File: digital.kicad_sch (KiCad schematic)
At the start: 29 parts, among them J1 Program Connector, J2 UART, J3 LCD ILI9488, SW1 Voltage, SW2 Current, U6 REF3030, U7 STM32G431CBTx

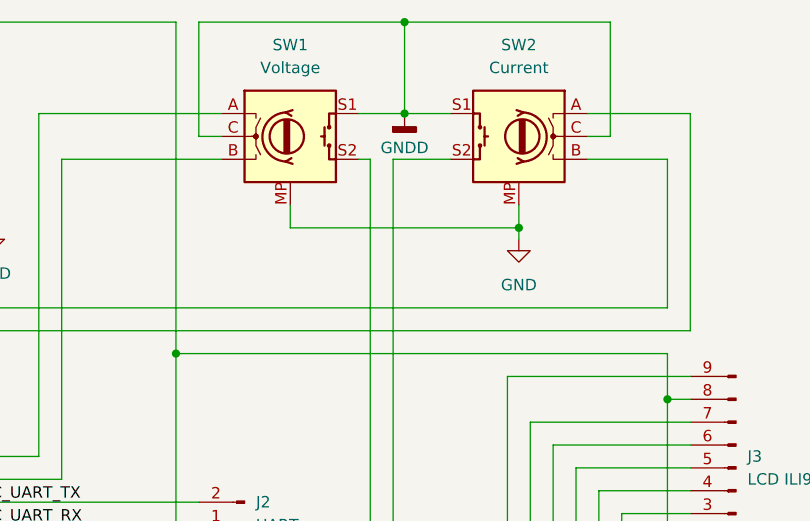
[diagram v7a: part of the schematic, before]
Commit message: Wstępne dodanie elementów na pcb oraz zmiana numeracji pinów do połączenia enkoderów. Zmiana symboli enkoderów na wersję bez masy i usunięcie zbędnego połączenia masy
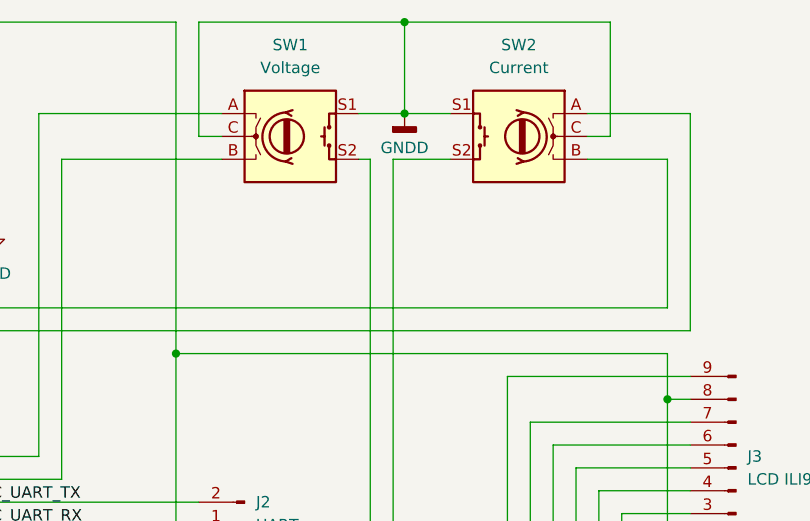
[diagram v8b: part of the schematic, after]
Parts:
- SW1, SW2: footprint (none) -> Connector_PinHeader_2.54mm:PinHeader_1x05_P2.54mm_Vertical; symbol Device:RotaryEncoder_Switch_MP -> Device:RotaryEncoder_Switch
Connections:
- net GND: no longer SW1.MP, SW2.MP
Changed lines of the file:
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@@
 		(color 0 0 0 0)
 	)
-	(junction
-		(at 222.25 41.91)
-		(diameter 0)
-		(color 0 0 0 0)
-	)
 	(no_connect
 		(at 125.73 85.09)
@@
 	(wire
 		(pts
-			(xy 222.25 41.91) (xy 222.25 39.37)
-		)
-		(stroke
-			(width 0)
-			(type default)
-		)
-	)
-	(wire
-		(pts
 			(xy 163.83 40.64) (xy 160.02 40.64)
 		)
@@
 	(wire
 		(pts
-			(xy 196.85 39.37) (xy 196.85 41.91)
-		)
-		(stroke
-			(width 0)
-			(type default)
-		)
-	)
-	(wire
-		(pts
 			(xy 186.69 19.05) (xy 209.55 19.05)
 		)
@@
 	(wire
 		(pts
-			(xy 196.85 41.91) (xy 222.25 41.91)
-		)
-		(stroke
-			(width 0)
-			(type default)
-		)
-	)
-	(wire
-		(pts
 			(xy 241.3 78.74) (xy 238.76 78.74)
 		)
@@
 	(wire
 		(pts
-			(xy 222.25 41.91) (xy 222.25 43.18)
-		)
-		(stroke
-			(width 0)
-			(type default)
-		)
-	)
-	(wire
-		(pts
 			(xy 246.38 105.41) (xy 246.38 110.49)
 		)
@@
 	)
 	(symbol
-		(lib_id "power:GND")
-		(at 222.25 43.18 0)
-		(unit 1)
-		(body_style 1)
-		(exclude_from_sim no)
-		(in_bom yes)
-		(on_board yes)
-		(in_pos_files yes)
-		(dnp no)
-		(fields_autoplaced yes)
-		(property "Reference" "#PWR027"
-			(at 222.25 49.53 0)
-			(hide yes)
-			(show_name no)
-			(do_not_autoplace no)
-			(effects
-				(font
-					(size 1.27 1.27)
-				)
-			)
-		)
-		(property "Value" "GND"
-			(at 222.25 48.26 0)
-			(show_name no)
-			(do_not_autoplace no)
-			(effects
-				(font
-					(size 1.27 1.27)
-				)
-			)
-		)
-		(property "Footprint" ""
-			(at 222.25 43.18 0)
-			(hide yes)
-			(show_name no)
-			(do_not_autoplace no)
-			(effects
-				(font
-					(size 1.27 1.27)
-				)
-			)
-		)
-		(property "Datasheet" ""
-			(at 222.25 43.18 0)
-			(hide yes)
-			(show_name no)
-			(do_not_autoplace no)
-			(effects
-				(font
-					(size 1.27 1.27)
-				)
-			)
-		)
-		(property "Description" "Power symbol creates a global label with name \"GND\" , ground"
-			(at 222.25 43.18 0)
-			(hide yes)
-			(show_name no)
-			(do_not_autoplace no)
-			(effects
-				(font
-					(size 1.27 1.27)
-				)
-			)
-		)
-		(pin "1"
-		)
-		(instances
-			(project ""
-				(path "/c7e56cf4-6d5c-4b1f-beec-285979763629"
-					(reference "#PWR03")
-					(unit 1)
-				)
-			)
-			(project "zasilacz_projekt_kompetencyjny"
-				(path "/e9ad3936-200e-4b7c-85fb-533ca6ea54fd/eba393f9-1041-42a1-a84c-5211747d5fcc"
-					(reference "#PWR027")
-					(unit 1)
-				)
-			)
-		)
-	)
-	(symbol
 		(lib_id "Device:R")
 		(at 148.59 25.4 0)
@@
 	)
 	(symbol
-		(lib_id "Device:RotaryEncoder_Switch_MP")
+		(lib_id "Device:RotaryEncoder_Switch")
 		(at 222.25 31.75 0)
 		(mirror y)
@@
 			)
 		)
-		(property "Footprint" ""
+		(property "Footprint" "Connector_PinHeader_2.54mm:PinHeader_1x05_P2.54mm_Vertical"
 			(at 226.06 27.686 0)
 			(hide yes)
@@
 		)
 		(property "Datasheet" ""
-			(at 222.25 44.45 0)
+			(at 222.25 25.146 0)
 			(hide yes)
 			(show_name no)
@@
 			)
 		)
-		(property "Description" "Rotary encoder, dual channel, incremental quadrate outputs, with switch and MP Pin"
-			(at 222.25 46.99 0)
+		(property "Description" "Rotary encoder, dual channel, incremental quadrate outputs, with switch"
+			(at 222.25 31.75 0)
 			(hide yes)
 			(show_name no)
@@
 		(pin "S1"
 		)
-		(pin "MP"
-		)
 		(pin "S2"
 		)
@@
 	)
 	(symbol
-		(lib_id "Device:RotaryEncoder_Switch_MP")
+		(lib_id "Device:RotaryEncoder_Switch")
 		(at 196.85 31.75 0)
 		(unit 1)
@@
 			)
 		)
-		(property "Footprint" ""
+		(property "Footprint" "Connector_PinHeader_2.54mm:PinHeader_1x05_P2.54mm_Vertical"
 			(at 193.04 27.686 0)
 			(hide yes)
@@
 		)
 		(property "Datasheet" ""
-			(at 196.85 44.45 0)
+			(at 196.85 25.146 0)
 			(hide yes)
 			(show_name no)
@@
 			)
 		)
-		(property "Description" "Rotary encoder, dual channel, incremental quadrate outputs, with switch and MP Pin"
-			(at 196.85 46.99 0)
+		(property "Description" "Rotary encoder, dual channel, incremental quadrate outputs, with switch"
+			(at 196.85 31.75 0)
 			(hide yes)
 			(show_name no)
@@
 		(pin "S1"
 		)
-		(pin "MP"
-		)
 		(pin "S2"
